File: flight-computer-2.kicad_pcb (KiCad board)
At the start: 4 copper layers, 51 x 51 mm, 79 parts, among them J1 USB4105-GF-A, J2 THR, J3 SER1, J4 SER2, J5 SER3, J6 SER4, J7 Breakout, SW1 RESET, SW2 BOOT, U1 AP2114H-3.3TRG1, U2 MUN5214DW1T1G, U3 BNO080, U4 CP2102N, U5 MPL3115A2, U6 ESP32-PICO-D4, Y1 32.768kHz

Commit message: Fix strapping pin being pulled high to prevent boot failure
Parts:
- R27: value 33k -> 27k
- R28: value 33k -> 47k
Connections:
- U6 pad 12: Net-(R22-Pad2) -> /EXT_PWR
- U6 pad 22: /EXT_PWR -> Net-(R22-Pad2)
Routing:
- net Net-(R22-Pad2): track 4.04 -> 10.3 mm, vias 0 -> 2
- net /EXT_PWR: track 13.4 -> 12.6 mm, vias 0 -> 2
- net GND: vias 81 -> 83

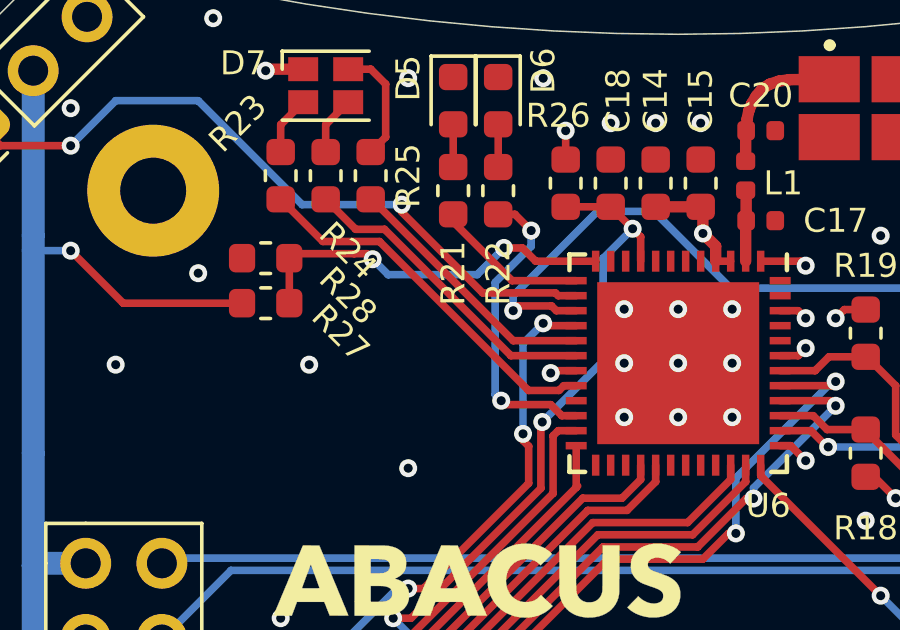
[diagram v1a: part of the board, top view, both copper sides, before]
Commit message: Better solution to strapping pin issue
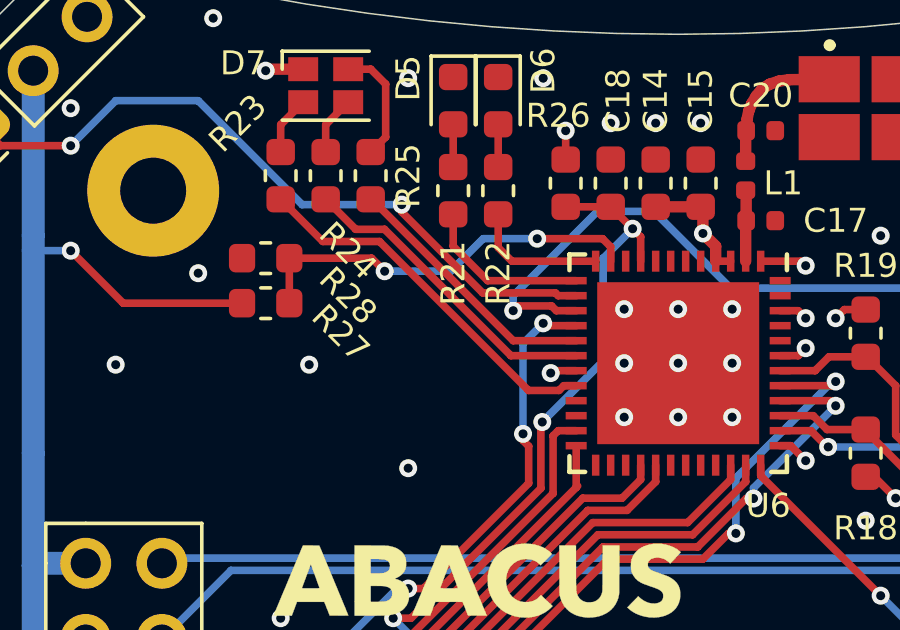
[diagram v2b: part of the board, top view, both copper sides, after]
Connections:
- U6 pad 11: (no net) -> /EXT_PWR
- U6 pad 12: /EXT_PWR -> Net-(R22-Pad2)
- U6 pad 22: Net-(R22-Pad2) -> (no net)
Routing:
- net Net-(R22-Pad2): track 10.3 -> 4.55 mm, vias 2 -> 0
- net /EXT_PWR: track 12.6 -> 13.4 mm
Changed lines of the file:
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@@
     (thickness 1.6)
     (drawings 16)
-    (tracks 660)
+    (tracks 649)
     (zones 0)
     (modules 79)
@@
     (pad 23 smd rect (at 2.25 3.4) (size 0.7 0.25) (layers F.Cu F.Paste F.Mask)
       (net 7 /IO0))
-    (pad 22 smd rect (at 1.75 3.4) (size 0.7 0.25) (layers F.Cu F.Paste F.Mask)
-      (net 52 "Net-(R22-Pad2)"))
+    (pad 22 smd rect (at 1.75 3.4) (size 0.7 0.25) (layers F.Cu F.Paste F.Mask))
     (pad 21 smd rect (at 1.25 3.4) (size 0.7 0.25) (layers F.Cu F.Paste F.Mask))
     (pad 20 smd rect (at 0.75 3.4) (size 0.7 0.25) (layers F.Cu F.Paste F.Mask)
@@
       (net 51 "Net-(R21-Pad2)"))
     (pad 12 smd rect (at -3.4 2.75 270) (size 0.7 0.25) (layers F.Cu F.Paste F.Mask)
+      (net 52 "Net-(R22-Pad2)"))
+    (pad 11 smd rect (at -3.4 2.25 270) (size 0.7 0.25) (layers F.Cu F.Paste F.Mask)
       (net 56 /EXT_PWR))
-    (pad 11 smd rect (at -3.4 2.25 270) (size 0.7 0.25) (layers F.Cu F.Paste F.Mask))
     (pad 10 smd rect (at -3.4 1.75 270) (size 0.7 0.25) (layers F.Cu F.Paste F.Mask))
     (pad 9 smd rect (at -3.4 1.25 270) (size 0.7 0.25) (layers F.Cu F.Paste F.Mask)
@@
   (segment (start 121.75 70.25) (end 120.371321 70.25) (width 0.254) (layer F.Cu) (net 50) (status 20))
   (via (at 121.75 70.25) (size 0.6) (drill 0.3) (layers F.Cu B.Cu) (net 50))
-  (segment (start 111.9625 53) (end 114.1 53) (width 0.254) (layer F.Cu) (net 51) (status 20))
-  (segment (start 110 51.0375) (end 111.9625 53) (width 0.254) (layer F.Cu) (net 51) (status 10))
-  (segment (start 110 50.7875) (end 110 51.0375) (width 0.254) (layer F.Cu) (net 51) (status 30))
-  (via (at 112.6 51.329652) (size 0.6) (drill 0.3) (layers F.Cu B.Cu) (net 52))
-  (segment (start 112.057848 50.7875) (end 112.6 51.329652) (width 0.254) (layer F.Cu) (net 52))
-  (segment (start 111.5 50.7875) (end 112.057848 50.7875) (width 0.254) (layer F.Cu) (net 52))
-  (segment (start 112.6 51.857514) (end 111.4 53.057514) (width 0.254) (layer B.Cu) (net 52))
-  (segment (start 112.6 51.329652) (end 112.6 51.857514) (width 0.254) (layer B.Cu) (net 52))
-  (via (at 111.6 57) (size 0.6) (drill 0.3) (layers F.Cu B.Cu) (net 52))
-  (segment (start 111.4 56.8) (end 111.6 57) (width 0.254) (layer B.Cu) (net 52))
-  (segment (start 111.4 53.057514) (end 111.4 56.8) (width 0.254) (layer B.Cu) (net 52))
-  (segment (start 113.622078 57.5) (end 114.1 57.5) (width 0.254) (layer F.Cu) (net 52))
-  (segment (start 113.254124 57.132046) (end 113.622078 57.5) (width 0.254) (layer F.Cu) (net 52))
-  (segment (start 111.732046 57.132046) (end 113.254124 57.132046) (width 0.254) (layer F.Cu) (net 52))
-  (segment (start 111.6 57) (end 111.732046 57.132046) (width 0.254) (layer F.Cu) (net 52))
+  (segment (start 110 50.7875) (end 110 51.8505) (width 0.254) (layer F.Cu) (net 51))
+  (segment (start 111.1495 53) (end 114.1 53) (width 0.254) (layer F.Cu) (net 51))
+  (segment (start 110 51.8505) (end 111.1495 53) (width 0.254) (layer F.Cu) (net 51))
+  (segment (start 111.5 50.7875) (end 111.5 51.89359) (width 0.254) (layer F.Cu) (net 52))
+  (segment (start 111.95641 52.35) (end 114.75 52.35) (width 0.254) (layer F.Cu) (net 52))
+  (segment (start 111.5 51.89359) (end 111.95641 52.35) (width 0.254) (layer F.Cu) (net 52))
   (segment (start 104.25 50.2875) (end 105.656285 51.693785) (width 0.254) (layer F.Cu) (net 53) (status 10))
   (segment (start 105.656285 51.693785) (end 107.544285 51.693785) (width 0.254) (layer F.Cu) (net 53))
@@
   (segment (start 112 55) (end 114.1 55) (width 0.254) (layer F.Cu) (net 55) (status 20))
   (segment (start 104.5375 53.75) (end 104.5375 52.25) (width 0.254) (layer F.Cu) (net 56) (status 30))
-  (segment (start 104.687305 52.100195) (end 104.5375 52.25) (width 0.254) (layer F.Cu) (net 56))
-  (segment (start 106.700195 52.100195) (end 104.687305 52.100195) (width 0.254) (layer F.Cu) (net 56))
-  (segment (start 107.131299 52.100195) (end 107.315552 52.284448) (width 0.254) (layer F.Cu) (net 56))
-  (via (at 107.315552 52.284448) (size 0.6) (drill 0.3) (layers F.Cu B.Cu) (net 56))
-  (segment (start 106.700195 52.100195) (end 107.131299 52.100195) (width 0.254) (layer F.Cu) (net 56))
-  (segment (start 107.315552 52.284448) (end 107.831104 52.8) (width 0.254) (layer B.Cu) (net 56))
-  (via (at 111.690948 51.909052) (size 0.6) (drill 0.3) (layers F.Cu B.Cu) (net 56))
-  (segment (start 110.8 52.8) (end 111.690948 51.909052) (width 0.254) (layer B.Cu) (net 56))
-  (segment (start 107.831104 52.8) (end 110.8 52.8) (width 0.254) (layer B.Cu) (net 56))
-  (segment (start 111.690948 51.909052) (end 112.309052 51.909052) (width 0.254) (layer F.Cu) (net 56))
-  (segment (start 112.75 52.35) (end 114.75 52.35) (width 0.254) (layer F.Cu) (net 56))
-  (segment (start 112.309052 51.909052) (end 112.75 52.35) (width 0.254) (layer F.Cu) (net 56))
+  (via (at 107.715552 52.684448) (size 0.6) (drill 0.3) (layers F.Cu B.Cu) (net 56))
+  (segment (start 107.281104 52.25) (end 107.715552 52.684448) (width 0.254) (layer F.Cu) (net 56))
+  (segment (start 104.5375 52.25) (end 107.281104 52.25) (width 0.254) (layer F.Cu) (net 56))
+  (segment (start 107.715552 52.684448) (end 109.915552 52.684448) (width 0.254) (layer B.Cu) (net 56))
+  (via (at 112.8 51.6) (size 0.6) (drill 0.3) (layers F.Cu B.Cu) (net 56))
+  (segment (start 111 51.6) (end 112.8 51.6) (width 0.254) (layer B.Cu) (net 56))
+  (segment (start 109.915552 52.684448) (end 111 51.6) (width 0.254) (layer B.Cu) (net 56))
+  (segment (start 115.25 51.872078) (end 115.25 52.35) (width 0.254) (layer F.Cu) (net 56))
+  (segment (start 114.977922 51.6) (end 115.25 51.872078) (width 0.254) (layer F.Cu) (net 56))
+  (segment (start 112.8 51.6) (end 114.977922 51.6) (width 0.254) (layer F.Cu) (net 56))
   (via (at 122.5 58.5419) (size 0.6) (drill 0.3) (layers F.Cu B.Cu) (net 57))
   (segment (start 122.46715 58.5419) (end 122.5 58.5419) (width 0.254) (layer F.Cu) (net 57))

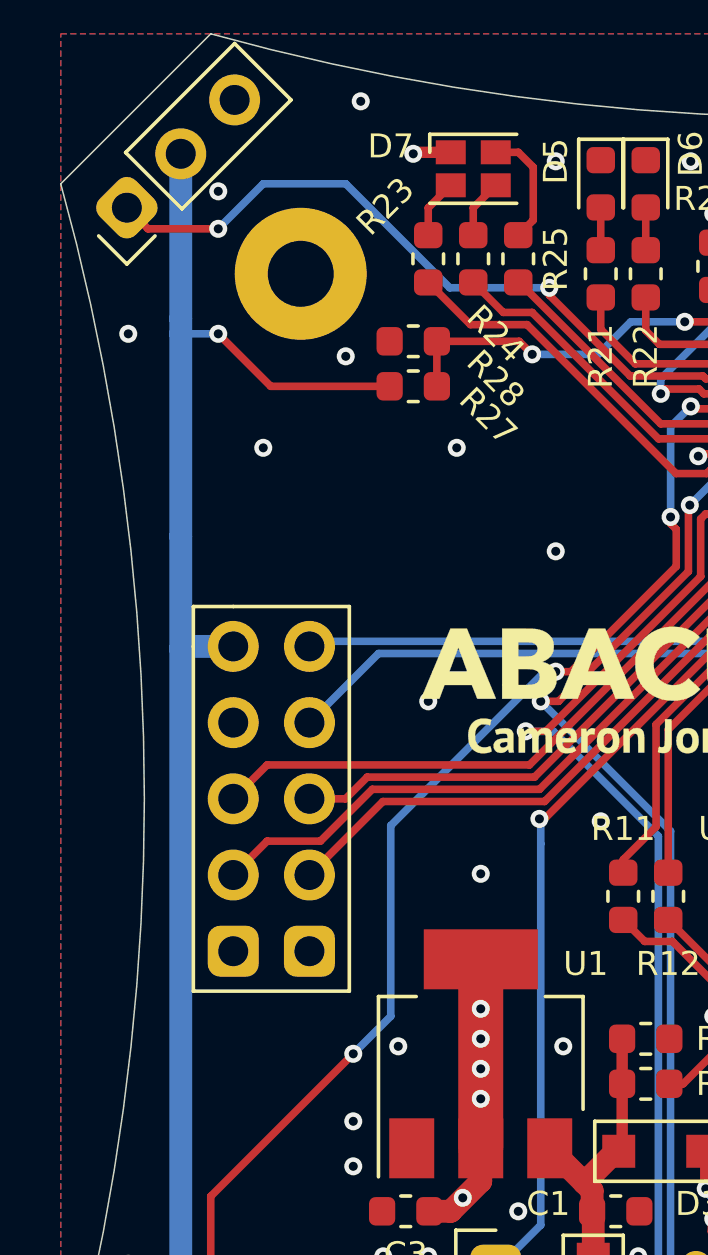
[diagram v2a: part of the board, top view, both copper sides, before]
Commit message: Small routing changes
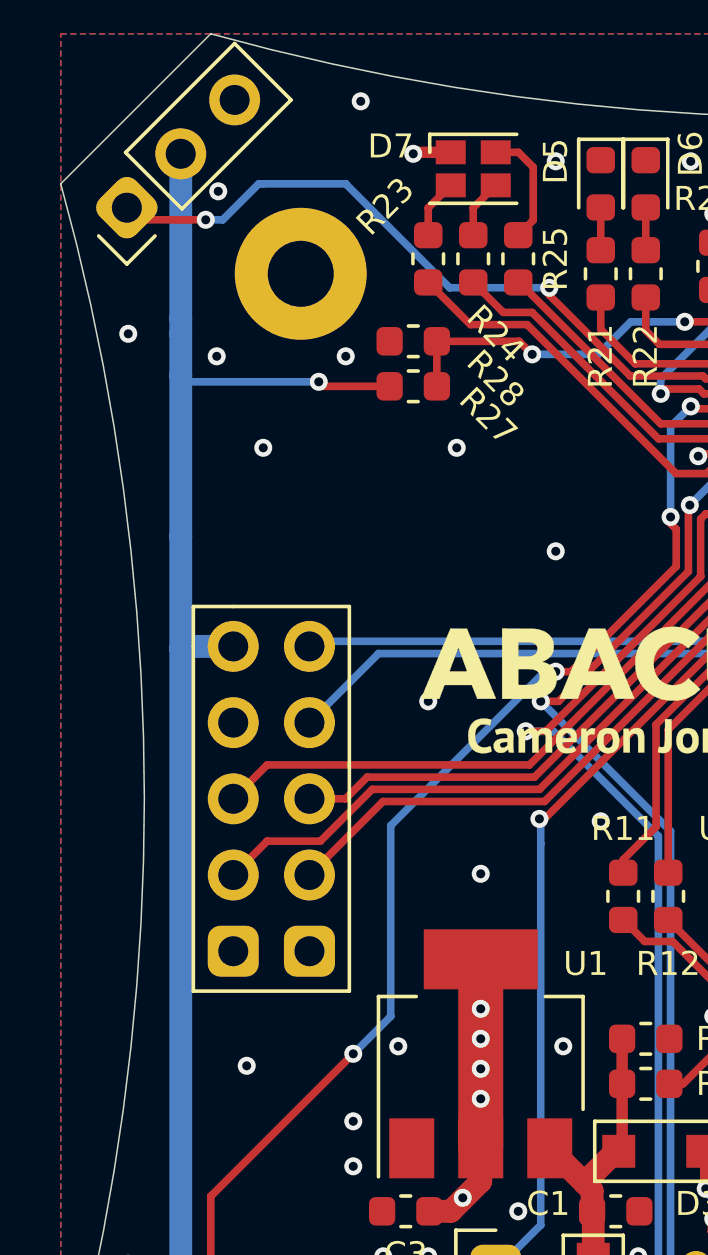
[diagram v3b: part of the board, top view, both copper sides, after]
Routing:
- net /VBEC: track 147.8 -> 147.2 mm
- net GND: vias 83 -> 85
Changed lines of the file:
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@@
     (thickness 1.6)
     (drawings 16)
-    (tracks 649)
+    (tracks 655)
     (zones 0)
     (modules 79)
@@
     (add_net "Net-(R9-Pad1)")
   )
+  (module Resistor_SMD:R_0603_1608Metric (layer F.Cu)
+    (at 103.75 53.75)
+    (descr "Resistor SMD 0603 (1608 Metric), square (rectangular) end terminal, IPC_7351 nominal, (Body size source: http://www.tortai-tech.com/upload/download/2011102023233369053.pdf), generated with kicad-footprint-generator")
+    (tags resistor)
+    (attr smd)
+    (fp_text reference R27 (at 2.5 1 135) (layer F.SilkS)
+      (effects (font (size 0.8 0.8) (thickness 0.18)))
+    )
+    (fp_text value 27k (at 0 1.43) (layer F.Fab)
+      (effects (font (size 1 1) (thickness 0.15)))
+    )
+    (fp_line (start 1.48 0.73) (end -1.48 0.73) (layer F.CrtYd) (width 0.05))
+    (fp_line (start 1.48 -0.73) (end 1.48 0.73) (layer F.CrtYd) (width 0.05))
+    (fp_line (start -1.48 -0.73) (end 1.48 -0.73) (layer F.CrtYd) (width 0.05))
+    (fp_line (start -1.48 0.73) (end -1.48 -0.73) (layer F.CrtYd) (width 0.05))
+    (fp_line (start -0.162779 0.51) (end 0.162779 0.51) (layer F.SilkS) (width 0.12))
+    (fp_line (start -0.162779 -0.51) (end 0.162779 -0.51) (layer F.SilkS) (width 0.12))
+    (fp_line (start 0.8 0.4) (end -0.8 0.4) (layer F.Fab) (width 0.1))
+    (fp_line (start 0.8 -0.4) (end 0.8 0.4) (layer F.Fab) (width 0.1))
+    (fp_line (start -0.8 -0.4) (end 0.8 -0.4) (layer F.Fab) (width 0.1))
+    (fp_line (start -0.8 0.4) (end -0.8 -0.4) (layer F.Fab) (width 0.1))
+    (fp_text user %R (at 0 0) (layer F.Fab)
+      (effects (font (size 0.4 0.4) (thickness 0.06)))
+    )
+    (pad 2 smd roundrect (at 0.7875 0) (size 0.875 0.95) (layers F.Cu F.Paste F.Mask) (roundrect_rratio 0.25)
+      (net 56 /EXT_PWR))
+    (pad 1 smd roundrect (at -0.7875 0) (size 0.875 0.95) (layers F.Cu F.Paste F.Mask) (roundrect_rratio 0.25)
+      (net 8 /VBEC))
+    (model ${KISYS3DMOD}/Resistor_SMD.3dshapes/R_0603_1608Metric.wrl
+      (at (xyz 0 0 0))
+      (scale (xyz 1 1 1))
+      (rotate (xyz 0 0 0))
+    )
+  )
   (module flight-computer-2:cj (layer F.Cu)
     (at 110.6 65.4)
@@
   )
   (module Resistor_SMD:R_0603_1608Metric (layer F.Cu)
-    (at 103.75 53.75)
-    (descr "Resistor SMD 0603 (1608 Metric), square (rectangular) end terminal, IPC_7351 nominal, (Body size source: http://www.tortai-tech.com/upload/download/2011102023233369053.pdf), generated with kicad-footprint-generator")
-    (tags resistor)
-    (attr smd)
-    (fp_text reference R27 (at 2.5 1 135) (layer F.SilkS)
-      (effects (font (size 0.8 0.8) (thickness 0.18)))
-    )
-    (fp_text value 27k (at 0 1.43) (layer F.Fab)
-      (effects (font (size 1 1) (thickness 0.15)))
-    )
-    (fp_line (start 1.48 0.73) (end -1.48 0.73) (layer F.CrtYd) (width 0.05))
-    (fp_line (start 1.48 -0.73) (end 1.48 0.73) (layer F.CrtYd) (width 0.05))
-    (fp_line (start -1.48 -0.73) (end 1.48 -0.73) (layer F.CrtYd) (width 0.05))
-    (fp_line (start -1.48 0.73) (end -1.48 -0.73) (layer F.CrtYd) (width 0.05))
-    (fp_line (start -0.162779 0.51) (end 0.162779 0.51) (layer F.SilkS) (width 0.12))
-    (fp_line (start -0.162779 -0.51) (end 0.162779 -0.51) (layer F.SilkS) (width 0.12))
-    (fp_line (start 0.8 0.4) (end -0.8 0.4) (layer F.Fab) (width 0.1))
-    (fp_line (start 0.8 -0.4) (end 0.8 0.4) (layer F.Fab) (width 0.1))
-    (fp_line (start -0.8 -0.4) (end 0.8 -0.4) (layer F.Fab) (width 0.1))
-    (fp_line (start -0.8 0.4) (end -0.8 -0.4) (layer F.Fab) (width 0.1))
-    (fp_text user %R (at 0 0) (layer F.Fab)
-      (effects (font (size 0.4 0.4) (thickness 0.06)))
-    )
-    (pad 2 smd roundrect (at 0.7875 0) (size 0.875 0.95) (layers F.Cu F.Paste F.Mask) (roundrect_rratio 0.25)
-      (net 56 /EXT_PWR))
-    (pad 1 smd roundrect (at -0.7875 0) (size 0.875 0.95) (layers F.Cu F.Paste F.Mask) (roundrect_rratio 0.25)
-      (net 8 /VBEC))
-    (model ${KISYS3DMOD}/Resistor_SMD.3dshapes/R_0603_1608Metric.wrl
-      (at (xyz 0 0 0))
-      (scale (xyz 1 1 1))
-      (rotate (xyz 0 0 0))
-    )
-  )
-  (module Resistor_SMD:R_0603_1608Metric (layer F.Cu)
     (at 103.75 52.25 180)
     (descr "Resistor SMD 0603 (1608 Metric), square (rectangular) end terminal, IPC_7351 nominal, (Body size source: http://www.tortai-tech.com/upload/download/2011102023233369053.pdf), generated with kicad-footprint-generator")
@@
   (via (at 105.2 55.8) (size 0.6) (drill 0.3) (layers F.Cu B.Cu) (net 1))
   (via (at 126 54.6) (size 0.6) (drill 0.3) (layers F.Cu B.Cu) (net 1))
+  (via (at 97.2 52.75) (size 0.6) (drill 0.3) (layers F.Cu B.Cu) (net 1))
+  (via (at 98.2 76.4) (size 0.6) (drill 0.3) (layers F.Cu B.Cu) (net 1))
   (segment (start 119.75 49.015) (end 119.75 48.015) (width 0.381) (layer F.Cu) (net 2) (status 30))
   (segment (start 119.765 48) (end 119.8 47.6) (width 0.381) (layer F.Cu) (net 2) (status 10))
@@
   (segment (start 96 58.75) (end 96 62.5) (width 0.762) (layer B.Cu) (net 8))
   (segment (start 96 46) (end 96 51.5) (width 0.762) (layer B.Cu) (net 8) (status 10))
-  (via (at 97.25 52) (size 0.6) (drill 0.3) (layers F.Cu B.Cu) (net 8))
-  (segment (start 96 51.5) (end 96 52) (width 0.762) (layer B.Cu) (net 8))
-  (segment (start 96 52) (end 97.25 52) (width 0.254) (layer B.Cu) (net 8))
-  (segment (start 96 52) (end 96 58.75) (width 0.762) (layer B.Cu) (net 8))
-  (segment (start 99 53.75) (end 102.9625 53.75) (width 0.254) (layer F.Cu) (net 8) (status 20))
-  (segment (start 97.25 52) (end 99 53.75) (width 0.254) (layer F.Cu) (net 8))
   (segment (start 106.35 85.6) (end 106.5 85.75) (width 0.762) (layer F.Cu) (net 8) (status 30))
   (segment (start 103.75 85.6) (end 106.35 85.6) (width 0.762) (layer F.Cu) (net 8) (status 30))
+  (segment (start 96 51.5) (end 96 52) (width 0.762) (layer B.Cu) (net 8))
+  (segment (start 96 53.4) (end 96 58.75) (width 0.762) (layer B.Cu) (net 8))
+  (segment (start 96 52) (end 96 53.4) (width 0.762) (layer B.Cu) (net 8))
+  (via (at 100.6 53.6) (size 0.6) (drill 0.3) (layers F.Cu B.Cu) (net 8))
+  (segment (start 100.75 53.75) (end 100.6 53.6) (width 0.254) (layer F.Cu) (net 8))
+  (segment (start 102.9625 53.75) (end 100.75 53.75) (width 0.254) (layer F.Cu) (net 8))
+  (segment (start 96.2 53.6) (end 96 53.4) (width 0.254) (layer B.Cu) (net 8))
+  (segment (start 100.6 53.6) (end 96.2 53.6) (width 0.254) (layer B.Cu) (net 8))
   (segment (start 109.2125 87.25) (end 109.2125 88.8) (width 0.254) (layer F.Cu) (net 9) (status 30))
   (segment (start 119.9 83.621506) (end 119.9 83.045) (width 0.381) (layer F.Cu) (net 10) (status 20))
@@
   (segment (start 114.823518 61.46923) (end 108.123521 68.169227) (width 0.254) (layer F.Cu) (net 23))
   (via (at 108.284698 50.465302) (size 0.6) (drill 0.3) (layers F.Cu B.Cu) (net 24))
-  (segment (start 108.284698 50.465302) (end 104.965302 50.465302) (width 0.254) (layer B.Cu) (net 24))
-  (segment (start 104.965302 50.465302) (end 101.5 47) (width 0.254) (layer B.Cu) (net 24))
-  (via (at 97.25 48.5) (size 0.6) (drill 0.3) (layers F.Cu B.Cu) (net 24))
-  (segment (start 98.75 47) (end 97.25 48.5) (width 0.254) (layer B.Cu) (net 24))
-  (segment (start 101.5 47) (end 98.75 47) (width 0.254) (layer B.Cu) (net 24))
-  (segment (start 94.203949 47.796051) (end 94.907898 48.5) (width 0.254) (layer F.Cu) (net 24) (status 10))
-  (segment (start 94.907898 48.5) (end 97.25 48.5) (width 0.254) (layer F.Cu) (net 24))
   (segment (start 113.40641 53.40641) (end 113.5 53.5) (width 0.254) (layer F.Cu) (net 24))
   (segment (start 113.5 53.5) (end 114.1 53.5) (width 0.254) (layer F.Cu) (net 24) (status 20))
@@
   (segment (start 110.98116 53.40641) (end 113.40641 53.40641) (width 0.254) (layer F.Cu) (net 24))
   (segment (start 108.284698 50.465302) (end 108.284698 50.709948) (width 0.254) (layer F.Cu) (net 24))
+  (segment (start 101.5 47) (end 98.75 47) (width 0.254) (layer B.Cu) (net 24))
+  (segment (start 108.284698 50.465302) (end 104.965302 50.465302) (width 0.254) (layer B.Cu) (net 24))
+  (segment (start 104.965302 50.465302) (end 101.5 47) (width 0.254) (layer B.Cu) (net 24))
+  (segment (start 98.75 47) (end 98.6 47) (width 0.254) (layer B.Cu) (net 24))
+  (via (at 96.8334 48.2) (size 0.6) (drill 0.3) (layers F.Cu B.Cu) (net 24))
+  (segment (start 97.4 48.2) (end 96.8334 48.2) (width 0.254) (layer B.Cu) (net 24))
+  (segment (start 98.6 47) (end 97.4 48.2) (width 0.254) (layer B.Cu) (net 24))
+  (segment (start 94.607898 48.2) (end 94.203949 47.796051) (width 0.254) (layer F.Cu) (net 24))
+  (segment (start 96.8334 48.2) (end 94.607898 48.2) (width 0.254) (layer F.Cu) (net 24))
   (segment (start 112.158801 53.841199) (end 112 54) (width 0.254) (layer F.Cu) (net 25))
   (segment (start 113.278113 53.841199) (end 112.158801 53.841199) (width 0.254) (layer F.Cu) (net 25))
@@
   (segment (start 97.75 67.5) (end 98.879401 66.370599) (width 0.254) (layer F.Cu) (net 34) (status 10))
   (segment (start 114.150159 59.843591) (end 114.15016 59.84359) (width 0.254) (layer F.Cu) (net 34))
-  (segment (start 114.1 59.89375) (end 114.1 58.5) (width 0.254) (layer F.Cu) (net 34) (status 20))
+  (segment (start 114.1 59.89375) (end 114.1 58.5) (width 0.254) (layer F.Cu) (net 34))
   (segment (start 107.623151 66.370599) (end 114.1 59.89375) (width 0.254) (layer F.Cu) (net 34))
   (segment (start 125.441901 80.154401) (end 125.25 79.9625) (width 0.254) (layer F.Cu) (net 35) (status 30))
